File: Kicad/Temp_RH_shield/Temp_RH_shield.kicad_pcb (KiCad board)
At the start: 2 copper layers, 12 parts, among them J1 Temp_RH_Module, J10 CONN_02X01, J2 micro_SD, J3 RTC, J4 Screw_Terminal_1x02, J5 CONN_01X01, J6 CONN_01X01, J7 CONN_01X01, J8 CONN_02X01, J9 CONN_02X01

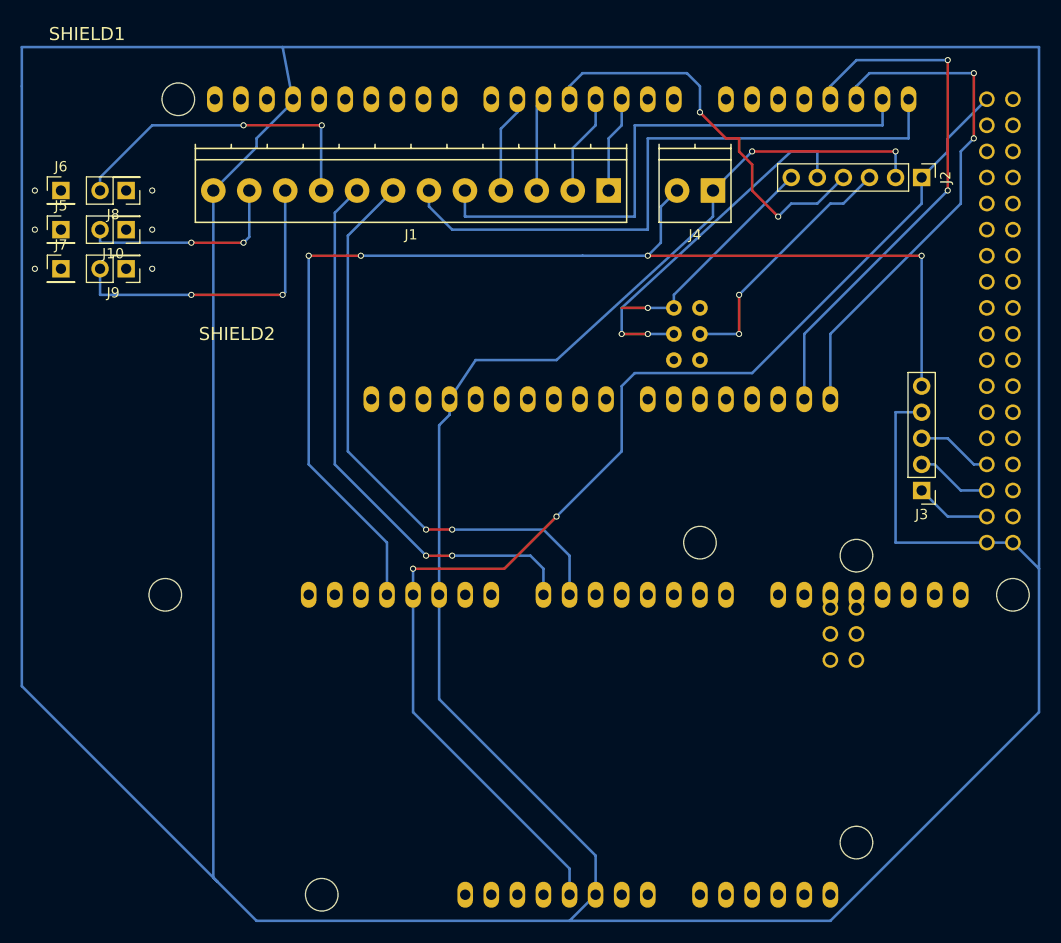
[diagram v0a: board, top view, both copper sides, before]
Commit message: Changes made on the file structure (not yet finished). Added Arduino project for Gas, Current, Motion, Reed and Distance sensors (GCMRD). Modifyed Temp_HR  shield to add the MLX sensor.
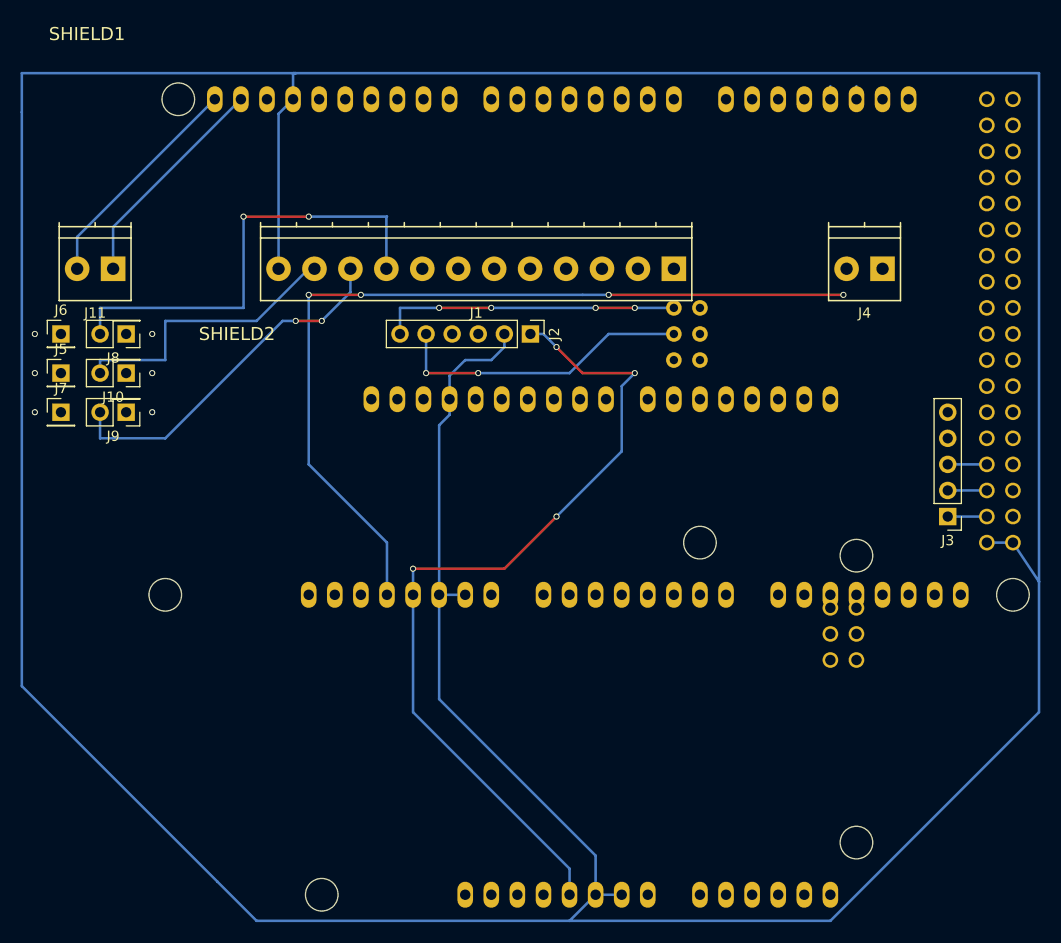
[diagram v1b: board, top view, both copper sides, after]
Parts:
- added J11: Screw_Terminal_1x02, Connectors_Terminal_Blocks:TerminalBlock_Pheonix_PT-3.5mm_2pol, F.Cu at (80.0, 67.3)
- moved J2 41.0 mm to (120.7, 73.7)
- moved J4 18.2 mm to (154.9, 67.3)
- moved J10 14.0 mm to (81.3, 77.5)
- moved J5 14.0 mm to (74.9, 77.5)
- moved J6 14.0 mm to (74.9, 73.7)
- moved J7 14.0 mm to (74.9, 81.3)
- moved J8 14.0 mm to (81.3, 73.7)
- moved J9 14.0 mm to (81.3, 81.3)
- moved J1 9.92 mm to (134.6, 67.3)
- moved J3 3.59 mm to (161.3, 91.4)
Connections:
- SHIELD1 pad SCL1: (no net) -> Net-(J11-Pad2)
- SHIELD1 pad SDA1: (no net) -> Net-(J11-Pad1)
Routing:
- net Net-(J1-Pad12): track 575.0 -> 439.0 mm, vias 2 -> 0
- net /SCL: track 61.9 -> 0.00 mm
- net /NTC_AN: track 56.8 -> 0.00 mm, vias 2 -> 0
- net /PT100_AN: track 54.6 -> 0.00 mm, vias 2 -> 0
- net /SDA: track 54.6 -> 0.00 mm
- net Net-(SHIELD1-Pad18): track 52.6 -> 1.27 mm, vias 2 -> 0
- net Net-(SHIELD1-Pad19): track 50.8 -> 1.27 mm, vias 2 -> 0
- net /uSD_CS: track 39.6 -> 0.00 mm, vias 2 -> 0
- net Net-(J2-Pad1): track 118.8 -> 83.0 mm, vias 2 -> 4
- net Net-(J3-Pad5): track 116.1 -> 84.4 mm
- net Net-(J2-Pad3): track 25.1 -> 0.00 mm, vias 2 -> 0
- net Net-(J11-Pad2): track 0.00 -> 22.1 mm
- net Net-(J11-Pad1): track 0.00 -> 21.7 mm
- net MAX31855_SO(MISO): track 31.3 -> 44.5 mm
- net /DHT22_DATA: track 9.81 -> 0.00 mm
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
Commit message: Added PT100 conditioning circuit to Tem_HR shield. Ready for testing!
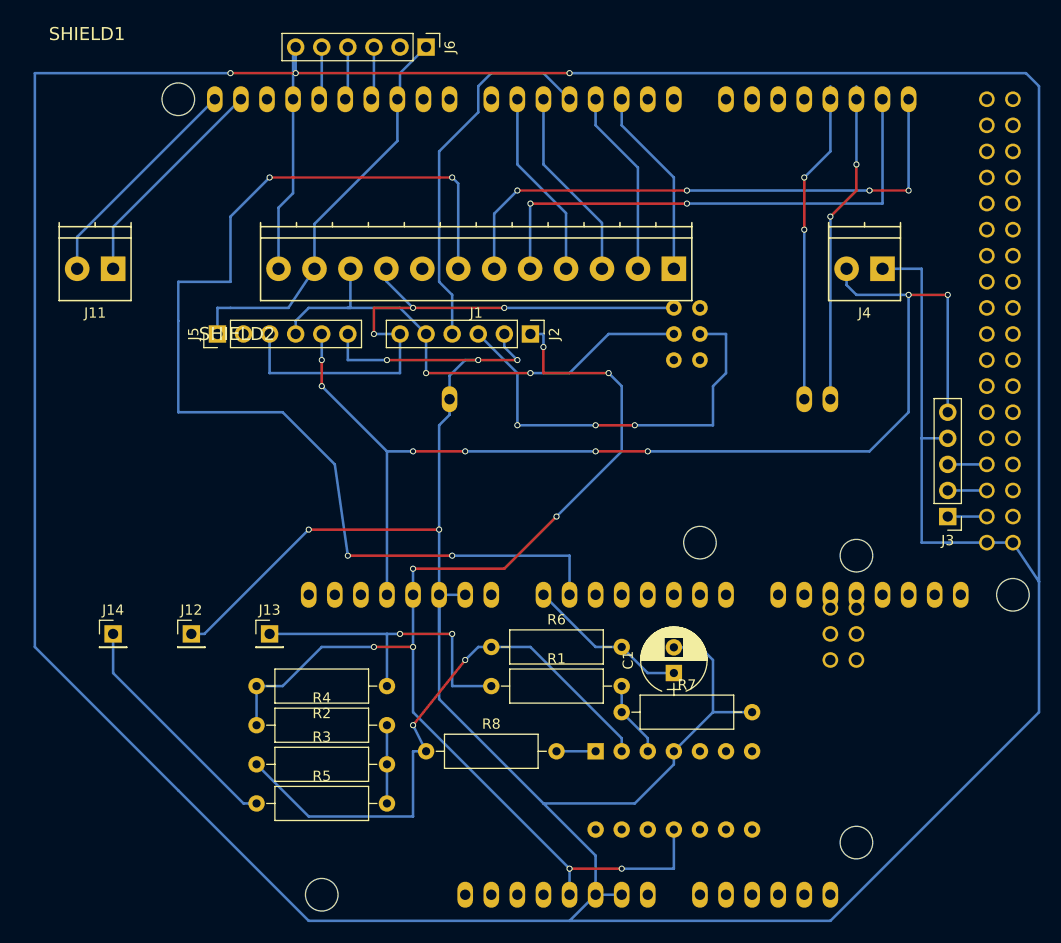
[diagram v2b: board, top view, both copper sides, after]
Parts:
- removed J10, J8, J9: CONN_02X01, Pin_Headers:Pin_Header_Straight_2x01_Pitch2.54mm
- removed J7: CONN_01X01, Pin_Headers:Pin_Header_Straight_1x01_Pitch2.54mm
- added C1: CP, Capacitors_THT:CP_Radial_D6.3mm_P2.50mm, F.Cu at (134.6, 106.7)
- added J12: CONN_01X01, Pin_Headers:Pin_Header_Straight_1x01_Pitch2.54mm, F.Cu at (87.6, 102.9)
- added J13: CONN_01X01, Pin_Headers:Pin_Header_Straight_1x01_Pitch2.54mm, F.Cu at (95.2, 102.9)
- added J14: CONN_01X01, Pin_Headers:Pin_Header_Straight_1x01_Pitch2.54mm, F.Cu at (80.0, 102.9)
- added R1: 4650, Resistors_THT:R_Axial_DIN0309_L9.0mm_D3.2mm_P12.70mm_Horizontal, F.Cu at (116.8, 108.0)
- added R2: 1779, Resistors_THT:R_Axial_DIN0309_L9.0mm_D3.2mm_P12.70mm_Horizontal, F.Cu at (106.7, 108.0)
- added R3: 4630, Resistors_THT:R_Axial_DIN0309_L9.0mm_D3.2mm_P12.70mm_Horizontal, F.Cu at (94.0, 115.6)
- added R4: 1787, Resistors_THT:R_Axial_DIN0309_L9.0mm_D3.2mm_P12.70mm_Horizontal, F.Cu at (94.0, 111.8)
- added R5: 98.8, Resistors_THT:R_Axial_DIN0309_L9.0mm_D3.2mm_P12.70mm_Horizontal, F.Cu at (94.0, 119.4)
- added R6: 9780, Resistors_THT:R_Axial_DIN0309_L9.0mm_D3.2mm_P12.70mm_Horizontal, F.Cu at (116.8, 104.1)
- added R7: 178000, Resistors_THT:R_Axial_DIN0309_L9.0mm_D3.2mm_P12.70mm_Horizontal, F.Cu at (129.5, 110.5)
- added R8: 180000, Resistors_THT:R_Axial_DIN0309_L9.0mm_D3.2mm_P12.70mm_Horizontal, F.Cu at (110.5, 114.3)
- added U1: LM324N, Housings_DIP:DIP-14_W7.62mm_Socket, B.Cu at (127.0, 114.3)
- J5: value CONN_01X01 -> MAX31855_HW; footprint Pin_Headers:Pin_Header_Straight_1x01_Pitch2.54mm -> Pin_Headers:Pin_Header_Straight_1x06_Pitch2.54mm
- J6: value CONN_01X01 -> MAX31855_SW; footprint Pin_Headers:Pin_Header_Straight_1x01_Pitch2.54mm -> Pin_Headers:Pin_Header_Straight_1x06_Pitch2.54mm
- moved J6 45.2 mm to (110.5, 45.7), turned to 270 degrees
- moved J5 15.7 mm to (90.2, 73.7), turned to 90 degrees
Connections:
- J1 pad 10: MAX31855_SCK -> MAX31855_SCK_HW
- J1 pad 12: Net-(J1-Pad12) -> MAX31855_GND
- J1 pad 8: /PT100_AN -> (no net)
- J1 pad 9: MAX31855_SO(MISO) -> MAX31855_SO(MISO)_HW
- J2 pad 2: Net-(J1-Pad12) -> MAX31855_GND
- J2 pad 5: Net-(J2-Pad5) -> MAX31855_SCK_HW
- J2 pad 6: Net-(J2-Pad6) -> MAX31855_SO(MISO)_HW
- J3 pad 4: Net-(J1-Pad12) -> MAX31855_GND
- J3 pad 5: Net-(J3-Pad5) -> MAX31855_VCC
- J4 pad 1: Net-(J1-Pad12) -> MAX31855_GND
- J4 pad 2: Net-(J3-Pad5) -> MAX31855_VCC
- J5 pad 1: (no net) -> MAX31855_CS
- J6 pad 1: (no net) -> MAX31855_CS
- SHIELD1 pad 10: (no net) -> MAX31855_CS
- SHIELD1 pad 11: (no net) -> MAX31855_SO(MISO)_SW
- SHIELD1 pad 12: (no net) -> MAX31855_SCK_SW
- SHIELD1 pad 13: (no net) -> MAX31855_VCC_SW
- SHIELD1 pad 3V3: Net-(J3-Pad5) -> MAX31855_VCC
- SHIELD1 pad GND1: Net-(J1-Pad12) -> MAX31855_GND
- SHIELD1 pad GND2: Net-(J1-Pad12) -> MAX31855_GND
- SHIELD1 pad GND3: Net-(J1-Pad12) -> MAX31855_GND
- SHIELD1 pad GND4: Net-(J1-Pad12) -> MAX31855_GND
- SHIELD1 pad GND5: Net-(J1-Pad12) -> MAX31855_GND
- SHIELD1 pad SP1: Net-(J2-Pad6) -> MAX31855_SO(MISO)_HW
- SHIELD1 pad SP3: Net-(J2-Pad5) -> MAX31855_SCK_HW
- SHIELD2 pad GND1: Net-(J1-Pad12) -> MAX31855_GND
- SHIELD2 pad GND2: Net-(J1-Pad12) -> MAX31855_GND
- SHIELD2 pad GND3: Net-(J1-Pad12) -> MAX31855_GND
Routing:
- net MAX31855_GND: track 0.00 -> 562.4 mm, vias 0 -> 8
- net Net-(J1-Pad12): track 439.0 -> 0.00 mm
- net MAX31855_VCC: track 0.00 -> 115.1 mm, vias 0 -> 8
- net /NTC_AN: track 0.00 -> 108.2 mm, vias 0 -> 4
- net Net-(J3-Pad5): track 84.4 -> 0.00 mm, vias 4 -> 0
- net MAX31855_SO(MISO)_HW: track 0.00 -> 59.5 mm, vias 0 -> 3
- net Net-(R3-Pad1): track 0.00 -> 56.7 mm, vias 0 -> 2
- net /SCL: track 0.00 -> 55.5 mm, vias 0 -> 4
- net /SDA: track 0.00 -> 50.8 mm, vias 0 -> 2
- net MAX31855_SCK_HW: track 0.00 -> 49.1 mm, vias 0 -> 2
- net MAX31855_SO(MISO): track 44.5 -> 0.00 mm, vias 2 -> 0
- net Net-(J2-Pad3): track 0.00 -> 41.5 mm, vias 0 -> 3
- net /uSD_CS: track 0.00 -> 36.7 mm
- net MAX31855_SCK: track 35.1 -> 0.00 mm, vias 2 -> 0
- net Net-(J2-Pad1): track 83.0 -> 117.3 mm, vias 4 -> 8
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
